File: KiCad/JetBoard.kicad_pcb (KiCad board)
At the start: 2 copper layers, 71 parts, among them SW1 SW_Push, U1 RP2040, U10 STM8S001J3M, U11 RT5715GQW, U12 BQ25185DLHR, U13 TPS2116DRL, U14 TPS2116DRL, U15 TPS2552DRVR, U16 ATGM336H-5N31, U3 W25Q16JVSSIQ, U4 Si5351A-B-GT, U5 TLV61070ADBVR, U7 TPS7A0533PDBZ, U9 TPS2552DRVR, X2 X1G0042110003_C3013793

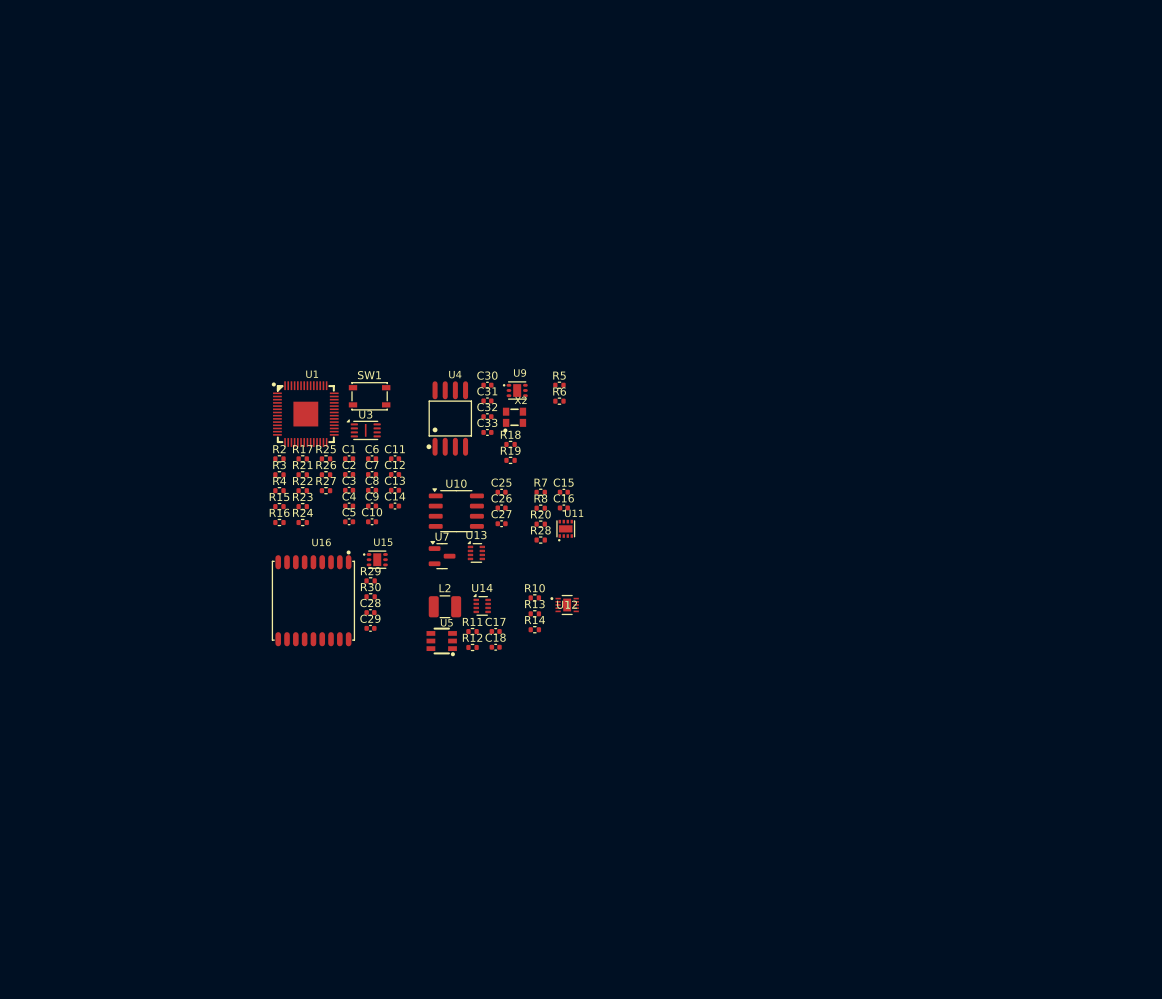
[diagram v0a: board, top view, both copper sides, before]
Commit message: Start of docs and design incremental progress
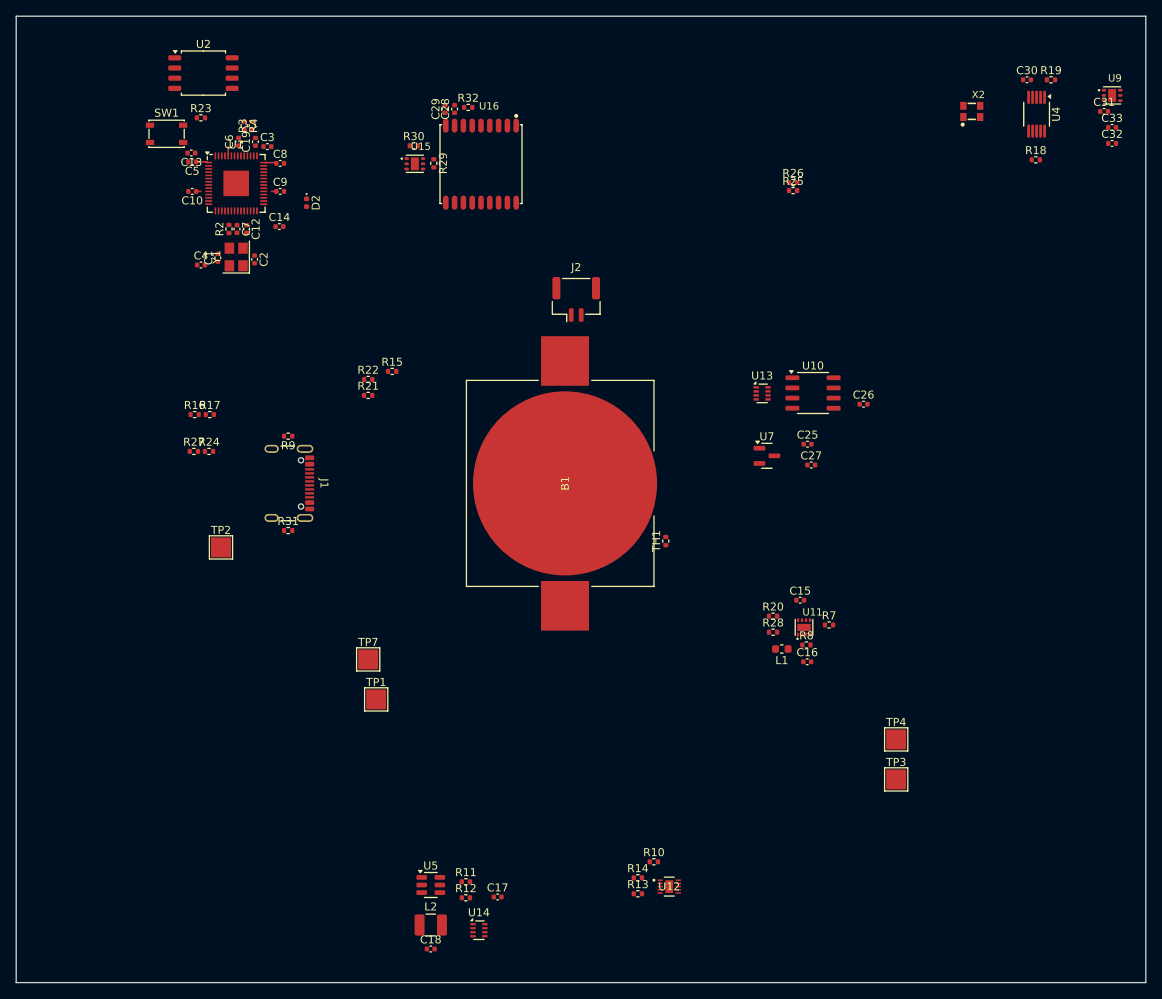
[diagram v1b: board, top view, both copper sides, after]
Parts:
- removed C11: 100nF, Capacitor_SMD:C_0402_1005Metric
- removed R5, R6: 5.1k, Resistor_SMD:R_0402_1005Metric
- removed U3: W25Q16JVSSIQ, Package_SON:Winbond_USON-8-1EP_3x2mm_P0.5mm_EP0.2x1.6mm
- added B1: BAT-HLD-006-SMT, JetBoard:BAT-HLD-006-SMT_LNX, F.Cu at (187.0, 101.0)
- added C19: 100nF, Capacitor_SMD:C_0402_1005Metric, F.Cu at (148.9, 58.3)
- added D2: LED_Small, LED_SMD:LED_0402_1005Metric, F.Cu at (155.3, 65.9)
- added J1: USB_C_Receptacle_USB2.0_16P, Connector_USB:USB_C_Receptacle_GCT_USB4105-xx-A_16P_TopMnt_Horizontal, F.Cu at (152.0, 101.0)
- added J2: Conn_01x02_Socket, Connector_JST:JST_GH_BM02B-GHS-TBT_1x02-1MP_P1.25mm_Vertical, F.Cu at (189.0, 78.0)
- added L1: 0.47uH, Inductor_SMD:L_0603_1608Metric, F.Cu at (214.7, 121.7)
- added R31: 5.1k, Resistor_SMD:R_0402_1005Metric, F.Cu at (153.0, 106.9)
- added R32: 10k, Resistor_SMD:R_0402_1005Metric, F.Cu at (175.5, 54.0)
- added R9: 5.1k, Resistor_SMD:R_0402_1005Metric, F.Cu at (153.0, 95.1)
- added TH1: 10k, Resistor_SMD:R_0402_1005Metric, F.Cu at (200.2, 108.2)
- added TP1: TestPoint, TestPoint:TestPoint_Pad_2.5x2.5mm, F.Cu at (164.0, 128.0)
- added TP2: TestPoint, TestPoint:TestPoint_Pad_2.5x2.5mm, F.Cu at (144.6, 109.0)
- added TP3: TestPoint, TestPoint:TestPoint_Pad_2.5x2.5mm, F.Cu at (229.0, 138.0)
- added TP4: TestPoint, TestPoint:TestPoint_Pad_2.5x2.5mm, F.Cu at (229.0, 133.0)
- added TP7: TestPoint, TestPoint:TestPoint_Pad_2.5x2.5mm, F.Cu at (163.0, 123.0)
- added U2: W25Q16JVSS, Package_SO:SOIC-8_5.3x5.3mm_P1.27mm, F.Cu at (142.4, 49.7)
- added Y1: 12.000MHz-ABM8-272-T3, Crystal:Crystal_SMD_3225-4Pin_3.2x2.5mm, F.Cu at (146.5, 72.7)
- U1: footprint JetBoard:LQFN-56_L7.0-W7.0-P0.4-EP -> Package_DFN_QFN:QFN-56-1EP_7x7mm_P0.4mm_EP3.2x3.2mm
- U4: footprint JetBoard:SOIC-8_L5.3-W5.3-P1.27-LS8.0-BL -> Package_SO:MSOP-10_3x3mm_P0.5mm
- U5: footprint JetBoard:SOT-23-6_L2.9-W1.6-P0.95-LS2.8-BR -> Package_TO_SOT_SMD:SOT-23-6
- moved C33 86.9 mm to (256.0, 56.5)
- moved C32 85.2 mm to (256.0, 58.5)
- moved C31 85.2 mm to (255.0, 54.5)
- moved U9 83.0 mm to (256.0, 52.5)
- moved R19 82.6 mm to (248.3, 50.6)
- moved U4 82.6 mm to (246.5, 54.9), turned to -90 degrees
- moved C30 77.5 mm to (245.3, 50.6)
- moved R18 74.7 mm to (246.4, 60.6)
- moved R26 68.9 mm to (216.1, 63.4)
- moved X2 68.8 mm to (238.4, 54.5)
- moved R25 67.3 mm to (216.1, 64.4)
- moved C29 65.6 mm to (172.6, 54.2), turned to 90 degrees
- moved C28 63.8 mm to (173.8, 54.2), turned to 90 degrees
- moved U16 58.5 mm to (177.1, 61.1)
- moved R30 56.6 mm to (168.7, 58.8)
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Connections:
- net +3.3V_GNSS renamed +3V3_GNSS
- net +V_BOOST renamed V_BOOST
- net /3V3 Buck/PI_RUN renamed /PI_RUN
- net /jetboard_gnss/GNSS_3V3_EN# renamed /jetboard_gnss/3V3_GNSS_EN#
- net /rp2040/USB_DP renamed /USB_DP
- net Net-(U10-VDD) renamed V_BAT_3V3
- net Net-(U5-EN) renamed /Solar Input/V_SOLAR
- C10 pad 1: +3.3V -> +3V3
- C14 pad 1: GND -> +3V3
- C15 pad 1: +3.3V -> +3V3
- C16 pad 1: +V_SYS -> V_SYS
- C3 pad 1: +3.3V -> +3V3
- C4 pad 1: +3.3V -> +3V3
- C5 pad 1: +3.3V -> +3V3
- C6 pad 1: +3.3V -> +3V3
- C7 pad 1: +3.3V -> +3V3
- C8 pad 1: +3.3V -> +3V3
- C9 pad 1: +3.3V -> +3V3
- R20 pad 2: +V_SYS -> V_SYS
- R21 pad 2: +3.3V -> +3V3
- R22 pad 2: +3.3V -> +3V3
- R25 pad 2: +3.3V -> +3V3
- R26 pad 2: +3.3V -> +3V3
- R28 pad 2: +3.3V -> +3V3
- R29 pad 1: +3.3V -> +3V3
- R30 pad 2: +3.3V -> +3V3
- R4 pad 1: /rp2040/USB_DM -> /USB_DM
- SW1 pad 2: (no net) -> GND
- U1 pad 1: +3.3V -> +3V3
- U1 pad 10: +3.3V -> +3V3
- U1 pad 16: /rp2040/STM8_SWIM -> /rp2040/STM8_SDA
- U1 pad 22: +3.3V -> +3V3
- U1 pad 33: +3.3V -> +3V3
- U1 pad 42: +3.3V -> +3V3
- U1 pad 43: +3.3V -> +3V3
- U1 pad 44: +3.3V -> +3V3
- U1 pad 48: +3.3V -> +3V3
- U1 pad 49: +3.3V -> +3V3
- U11 pad 5: +3.3V -> +3V3
- U11 pad 8: +V_SYS -> V_SYS
- U12 pad 1: +V_SYS -> V_SYS
- U13 pad 3: USB_VBUS -> V_SYS
- U14 pad 2: +V_SYS -> V_SYS
- U14 pad 7: +V_SYS -> V_SYS
- U15 pad 6: +3.3V -> +3V3
- U16 pad 6: /jetboard_gnss/GNSS_VBAT -> VBAT_3V3
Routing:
- net +3V3: track 0.00 -> 4.40 mm
- net /rp2040/QSPI_CLK: track 0.00 -> 1.05 mm
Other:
- board outline added: 141.2 x 120.8 mm

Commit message: Update schematic and board
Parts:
- added H1: MountingHole, MountingHole:ToolingHole_1.152mm, F.Cu at (149.7, 103.4)
- added H2: MountingHole, MountingHole:ToolingHole_1.152mm, F.Cu at (144.2, 103.0)
- J2: footprint Connector_JST:JST_GH_BM02B-GHS-TBT_1x02-1MP_P1.25mm_Vertical -> Connector_JST:JST_GH_SM02B-GHS-TB_1x02-1MP_P1.25mm_Horizontal
- TP3, TP4: footprint TestPoint:TestPoint_Pad_2.5x2.5mm -> TestPoint:TestPoint_Pad_1.5x1.5mm
- U11: footprint JetBoard:WDFN-8_L2.0-W2.0-P0.50-BL-EP -> Package_DFN_QFN:WDFN-8-1EP_2x2mm_P0.5mm_EP0.8x1.2mm
- U2: value W25Q16JVSS -> W25Q16JVUXIQ; footprint Package_SO:SOIC-8_5.3x5.3mm_P1.27mm -> Package_SON:Winbond_USON-8-1EP_3x2mm_P0.5mm_EP0.2x1.6mm
- U5: footprint Package_TO_SOT_SMD:SOT-23-6 -> JetBoard:SOT-23-6_L2.9-W1.6-P0.95-LS2.8-BR
- moved C33 130.9 mm to (133.7, 103.3)
- moved C31 125.9 mm to (140.6, 107.2), turned to 180 degrees
- moved U9 124.2 mm to (143.9, 106.0)
- moved C32 123.5 mm to (141.9, 105.9), turned to -90 degrees
- moved R19 122.2 mm to (140.6, 108.3), turned to 180 degrees
- moved C30 121.3 mm to (135.7, 102.5), turned to 180 degrees
- moved U4 119.3 mm to (138.3, 104.9), turned to 0 degrees
- moved X2 116.5 mm to (133.6, 105.2)
- moved R18 110.3 mm to (145.9, 106.0), turned to -90 degrees
- moved TP3 92.7 mm to (142.9, 103.5), turned to 180 degrees
- moved R25 89.9 mm to (137.3, 107.7), turned to -90 degrees
- moved R26 89.0 mm to (138.9, 107.7), turned to -90 degrees
- moved C26 88.7 mm to (136.7, 100.2)
- moved TP4 86.8 mm to (147.3, 103.4), turned to 180 degrees
- moved C25 79.6 mm to (138.4, 100.1)
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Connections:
- net /jetboard_gnss/3V3_GNSS_EN# renamed /gnss/3V3_GNSS_EN#
- net /jetboard_gnss/GNSS_1PPS renamed /gnss/GNSS_1PPS
- net /jetboard_gnss/GNSS_ANT renamed /gnss/GNSS_ANT
- net /jetboard_gnss/GNSS_RESET# renamed /gnss/GNSS_RESET#
- net /jetboard_gnss/GNSS_UART_RX renamed /gnss/GNSS_UART_RX
- net /jetboard_gnss/GNSS_UART_TX renamed /gnss/GNSS_UART_TX
- C31 pad 1: +3.3V_WSPR -> +3V3_WSPR
- C32 pad 1: +3.3V_WSPR -> +3V3_WSPR
- C33 pad 1: +3.3V_WSPR -> +3V3_WSPR
- J1 pad A6: Net-(J1-D+-PadA6) -> /USB_DP
- J1 pad B6: Net-(J1-D+-PadA6) -> /USB_DP
- R18 pad 1: +3.3V -> +3V3
- U9 pad 1: +3.3V_WSPR -> +3V3_WSPR
- U9 pad 6: +3.3V -> +3V3
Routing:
- net /USB_DP: track 0.00 -> 3.67 mm
- net /USB_DM: track 0.00 -> 3.66 mm
- net +3V3_GNSS: track 0.00 -> 2.80 mm
- net +3V3: track 4.40 -> 2.27 mm
- net VBAT_3V3: track 0.00 -> 1.57 mm
- net GND: track 0.00 -> 1.20 mm
- net /rp2040/QSPI_CLK: track 1.05 -> 0.00 mm
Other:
- board size 141.2 x 120.8 mm -> 41.6 x 57.3 mm
- copper layers 2 -> 4

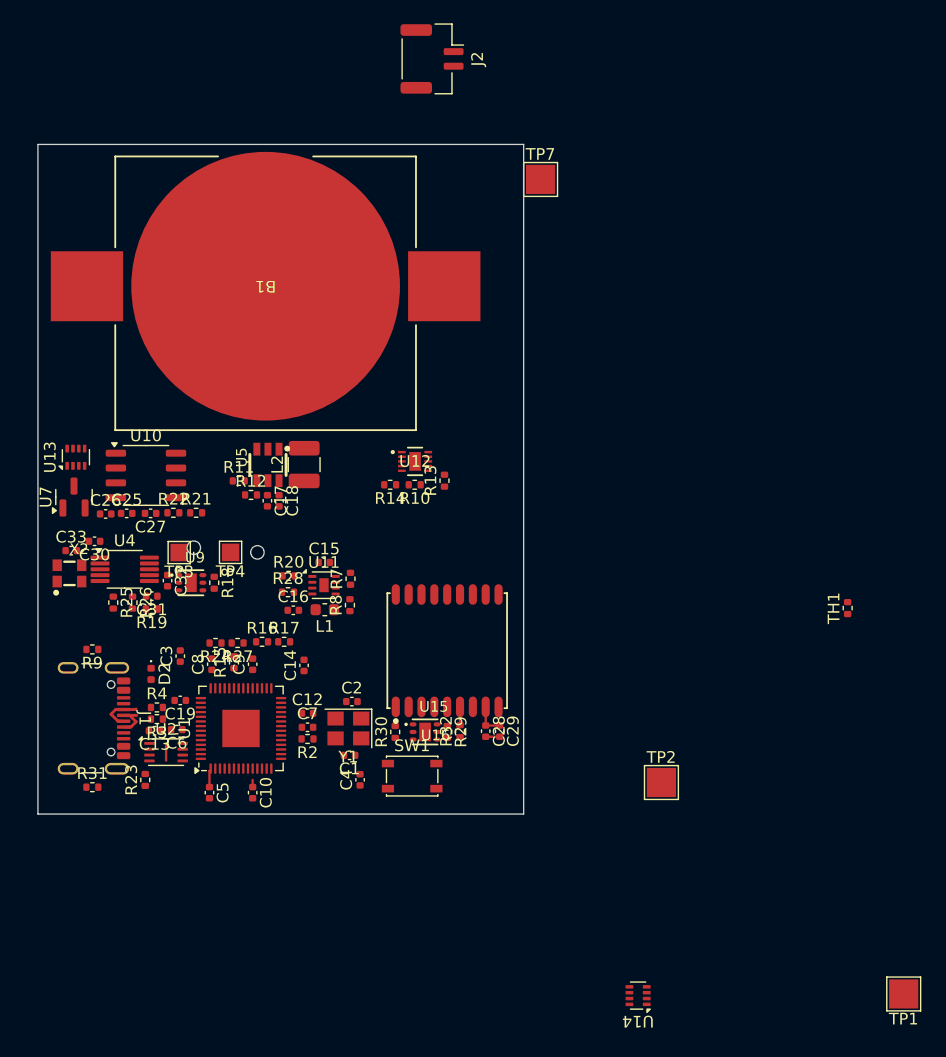
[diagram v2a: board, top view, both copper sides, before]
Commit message: Schematic and PCB updates
- Add basic solar modules and 3d step
- shrink PCB size
- need to find USB connector that doesn't go through the board
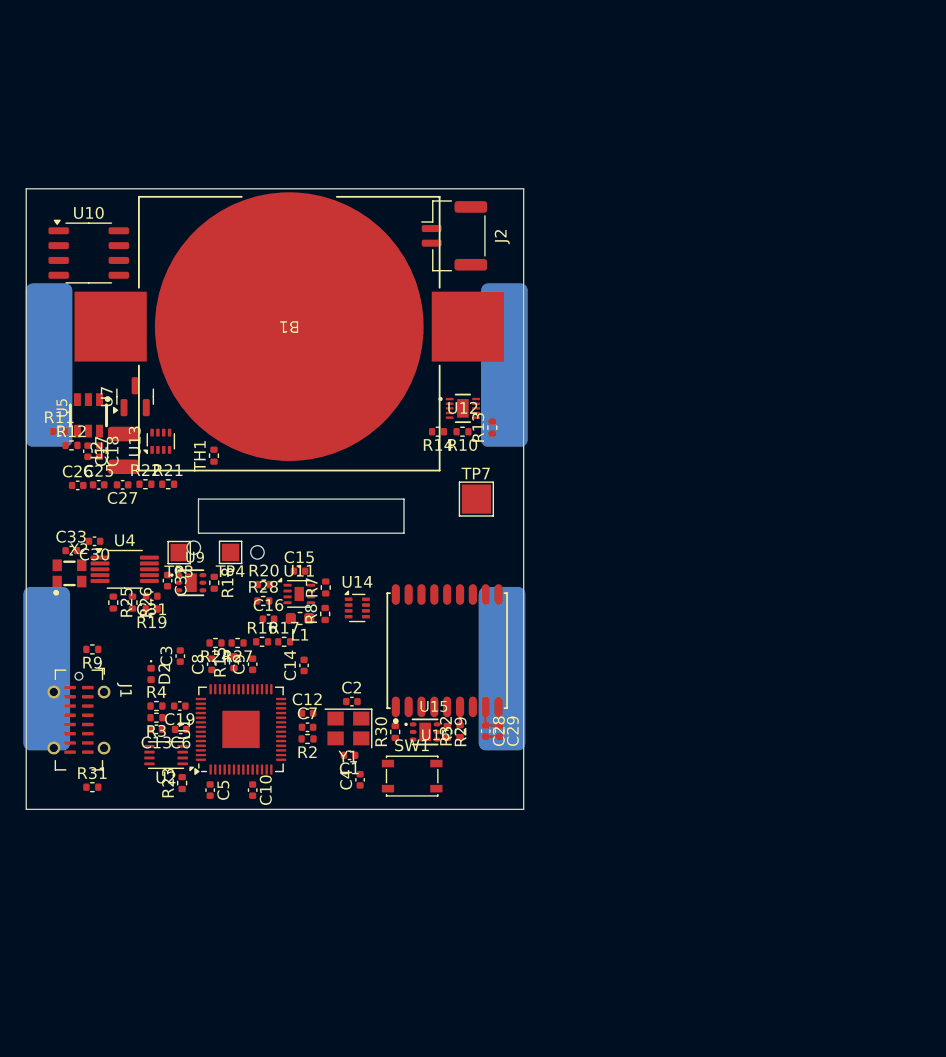
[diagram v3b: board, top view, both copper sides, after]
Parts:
- removed TP1, TP2: TestPoint, TestPoint:TestPoint_Pad_2.5x2.5mm
- added SC1: Solar_Cell, JetBoard:KXOB201K04TF, B.Cu at (151.8, 87.4)
- added SC2: Solar_Cell, JetBoard:KXOB201K04TF, B.Cu at (150.6, 113.4)
- J1: footprint Connector_USB:USB_C_Receptacle_GCT_USB4105-xx-A_16P_TopMnt_Horizontal -> Connector_USB:USB_C_Receptacle_G-Switch_GT-USB-7051x
- J2: footprint Connector_JST:JST_GH_SM02B-GHS-TB_1x02-1MP_P1.25mm_Horizontal -> Connector_JST:JST_GH_BM02B-GHS-TBT_1x02-1MP_P1.25mm_Vertical
- moved TH1 55.8 mm to (145.9, 95.2)
- moved U14 41.0 mm to (158.2, 108.2), turned to 0 degrees
- moved TP7 27.9 mm to (168.4, 98.9)
- moved U10 19.7 mm to (135.2, 77.8)
- moved U5 16.0 mm to (135.2, 91.7)
- moved C17 16.0 mm to (135.1, 94.8)
- moved C18 16.0 mm to (136.1, 94.8)
- moved R11 16.0 mm to (132.7, 93.1)
- moved R12 16.0 mm to (133.7, 94.3)
- moved L2 15.5 mm to (138.2, 94.7)
- moved J2 15.3 mm to (166.5, 76.3)
- moved U7 10.1 mm to (139.2, 90.1)
- moved U13 7.40 mm to (141.4, 93.9)
- moved R10 6.12 mm to (167.2, 93.1)
- moved U12 6.12 mm to (167.2, 91.1)
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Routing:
- net /USB_DP: track 3.67 -> 0.00 mm
- net /USB_DM: track 3.66 -> 0.00 mm
- net +3V3: track 2.27 -> 0.14 mm
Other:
- board size 41.6 x 57.3 mm -> 42.6 x 53.2 mm
